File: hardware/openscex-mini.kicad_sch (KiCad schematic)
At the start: 11 parts, among them J1 ISP, U1 ATtiny85-20PU

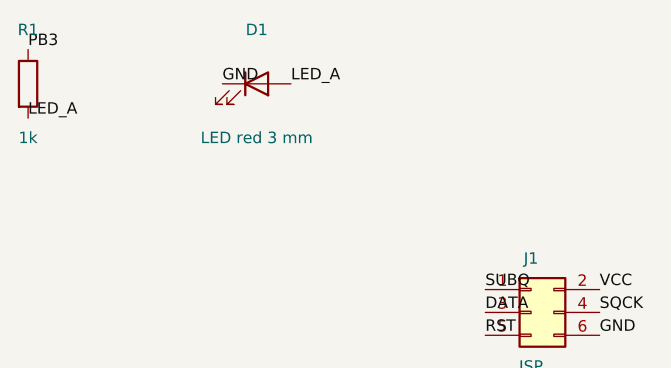
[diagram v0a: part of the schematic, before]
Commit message: feat(hardware): add a RESET pull-up to every board
The mini and bare boards now hold pin 1 high with a 10 kOhm pull-up,
as the carrier already did. The chip's own pull-up is 30 to 60 kOhm,
weak against noise coupled in from the console, and a spurious reset
costs the region check of the disc being read. Any ISP programmer
still overrides it.
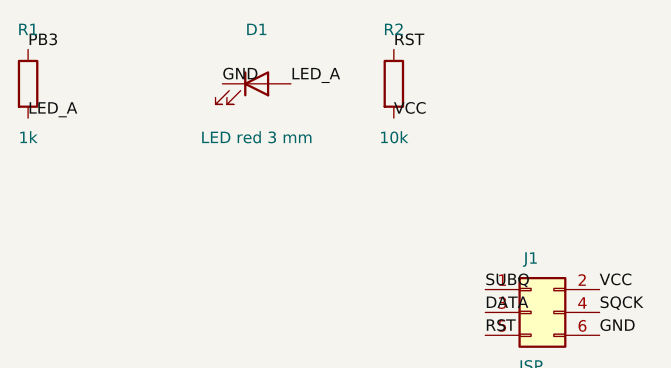
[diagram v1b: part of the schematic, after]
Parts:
- added R2: 10k, Resistor_THT:R_Axial_DIN0204_L3.6mm_D1.6mm_P5.08mm_Horizontal, symbol Device:R
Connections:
- net RST: now also R2.1
- net VCC: now also R2.2
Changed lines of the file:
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@@
 (kicad_sch (version 20231120) (generator "eeschema") (generator_version "8.0")
 	(paper "A3")
-	(title_block (title "openscex mini") (comment 1 "ATtiny85 PS1 modchip minimal carrier: socket, decoupling, LED, ISP"))
+	(title_block (title "openscex mini") (comment 1 "ATtiny85 PS1 modchip minimal carrier: socket, decoupling, RESET pull-up, LED, ISP"))
 (symbol (lib_id "MCU_Microchip_ATtiny:ATtiny85-20P") (at 76.2 76.2 0) (unit 1)
 	(in_bom yes) (on_board yes) (dnp no)
@@
 (label "VCC" (at 38.1 72.39 0) (effects (font (size 1.27 1.27)) (justify left bottom)))
 (label "GND" (at 38.1 80.01 0) (effects (font (size 1.27 1.27)) (justify left bottom)))
+(symbol (lib_id "Device:R") (at 167.64000000000001 50.8 0) (unit 1)
+	(in_bom yes) (on_board yes) (dnp no)
+	(property "Reference" "R2" (at 167.64000000000001 44.8 0) (effects (font (size 1.27 1.27))))
+	(property "Value" "10k" (at 167.64000000000001 56.8 0) (effects (font (size 1.27 1.27))))
+	(property "Footprint" "Resistor_THT:R_Axial_DIN0204_L3.6mm_D1.6mm_P5.08mm_Horizontal" (at 167.64000000000001 50.8 0) (effects (font (size 1.27 1.27)) (hide yes)))
+	(property "Datasheet" "" (at 167.64000000000001 50.8 0) (effects (font (size 1.27 1.27)) (hide yes)))
+	(property "Part" "10 kOhm axial resistor, DIN0204, 5.08 mm pitch" (at 167.64000000000001 50.8 0) (effects (font (size 1.27 1.27)) (hide yes)))
+	(pin "1")
+	(pin "2")
+	(instances (project "openscex-mini" (path "/7206801e-1c20-5311-8a84-3899543930cc" (reference "R2") (unit 1))))
+)
+(label "RST" (at 167.64 46.99 0) (effects (font (size 1.27 1.27)) (justify left bottom)))
+(label "VCC" (at 167.64 54.61 0) (effects (font (size 1.27 1.27)) (justify left bottom)))
 (symbol (lib_id "Device:R") (at 127.0 50.8 0) (unit 1)
 	(in_bom yes) (on_board yes) (dnp no)

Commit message: feat(hardware): name datasheet-checked parts
Every BOM line now names an exact manufacturer part, each checked
against its own datasheet: Microchip ATTINY85-20PU in a TE
1-2199298-2 socket, KEMET C315C104K5R5TA, Panasonic EEU-FC1A101S,
Vishay MBA0204 resistors, onsemi 2N3904RLRAG and 1N4148TR,
Kingbright WP710A10ID, CTS 206-2ST, Same Sky CMI-1295IC-0385T and
Wurth 61200621621.

C1 moves to a 4.0 x 2.5 mm footprint that fits the KEMET body. A
project footprint library, hardware/openscex.pretty, carries the hole
sizes the Wurth header and the buzzer datasheets recommend, 1.1 mm and
0.8 mm in 2 mm pads.
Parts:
- C1: footprint Capacitor_THT:C_Disc_D3.0mm_W1.6mm_P2.50mm -> Capacitor_THT:C_Rect_L4.0mm_W2.5mm_P2.50mm; Part 100 nF ceramic disc, 50 V, 2.5 mm pitch -> KEMET C315C104K5R5TA, 100 nF 50 V X7R, 2.54 mm
- D1: Part 3 mm red LED -> Kingbright WP710A10ID, 3 mm red LED
- J1: footprint Connector_IDC:IDC-Header_2x03_P2.54mm_Vertical -> openscex:IDC-Header_2x03_P2.54mm_Vertical_Wurth_61200621621; Part 2x3 shrouded box header, 2.54 mm, vertical -> Wurth 61200621621, 2x3 box header, 2.54 mm
- R1: Part 1 kOhm axial resistor, DIN0204, 5.08 mm pitch -> Vishay MBA02040C1001FC100, 1 kOhm 1 % 0.4 W, 0204
- R2: Part 10 kOhm axial resistor, DIN0204, 5.08 mm pitch -> Vishay MBA02040C1002FC100, 10 kOhm 1 % 0.4 W, 0204
- U1: Part ATtiny85-20PU in a DIP-8 7.62 mm socket -> Microchip ATTINY85-20PU in a TE 1-2199298-2 DIP-8 socket
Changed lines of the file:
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@@
 	(property "Footprint" "Package_DIP:DIP-8_W7.62mm_Socket" (at 76.2 76.2 0) (effects (font (size 1.27 1.27)) (hide yes)))
 	(property "Datasheet" "" (at 76.2 76.2 0) (effects (font (size 1.27 1.27)) (hide yes)))
-	(property "Part" "ATtiny85-20PU in a DIP-8 7.62 mm socket" (at 76.2 76.2 0) (effects (font (size 1.27 1.27)) (hide yes)))
+	(property "Part" "Microchip ATTINY85-20PU in a TE 1-2199298-2 DIP-8 socket" (at 76.2 76.2 0) (effects (font (size 1.27 1.27)) (hide yes)))
 	(pin "1")
 	(pin "2")
@@
 	(property "Reference" "C1" (at 38.1 70.2 0) (effects (font (size 1.27 1.27))))
 	(property "Value" "100nF" (at 38.1 82.2 0) (effects (font (size 1.27 1.27))))
-	(property "Footprint" "Capacitor_THT:C_Disc_D3.0mm_W1.6mm_P2.50mm" (at 38.1 76.2 0) (effects (font (size 1.27 1.27)) (hide yes)))
+	(property "Footprint" "Capacitor_THT:C_Rect_L4.0mm_W2.5mm_P2.50mm" (at 38.1 76.2 0) (effects (font (size 1.27 1.27)) (hide yes)))
 	(property "Datasheet" "" (at 38.1 76.2 0) (effects (font (size 1.27 1.27)) (hide yes)))
-	(property "Part" "100 nF ceramic disc, 50 V, 2.5 mm pitch" (at 38.1 76.2 0) (effects (font (size 1.27 1.27)) (hide yes)))
+	(property "Part" "KEMET C315C104K5R5TA, 100 nF 50 V X7R, 2.54 mm" (at 38.1 76.2 0) (effects (font (size 1.27 1.27)) (hide yes)))
 	(pin "1")
 	(pin "2")
@@
 	(property "Footprint" "Resistor_THT:R_Axial_DIN0204_L3.6mm_D1.6mm_P5.08mm_Horizontal" (at 167.64000000000001 50.8 0) (effects (font (size 1.27 1.27)) (hide yes)))
 	(property "Datasheet" "" (at 167.64000000000001 50.8 0) (effects (font (size 1.27 1.27)) (hide yes)))
-	(property "Part" "10 kOhm axial resistor, DIN0204, 5.08 mm pitch" (at 167.64000000000001 50.8 0) (effects (font (size 1.27 1.27)) (hide yes)))
+	(property "Part" "Vishay MBA02040C1002FC100, 10 kOhm 1 % 0.4 W, 0204" (at 167.64000000000001 50.8 0) (effects (font (size 1.27 1.27)) (hide yes)))
 	(pin "1")
 	(pin "2")
@@
 	(property "Footprint" "Resistor_THT:R_Axial_DIN0204_L3.6mm_D1.6mm_P5.08mm_Horizontal" (at 127.0 50.8 0) (effects (font (size 1.27 1.27)) (hide yes)))
 	(property "Datasheet" "" (at 127.0 50.8 0) (effects (font (size 1.27 1.27)) (hide yes)))
-	(property "Part" "1 kOhm axial resistor, DIN0204, 5.08 mm pitch" (at 127.0 50.8 0) (effects (font (size 1.27 1.27)) (hide yes)))
+	(property "Part" "Vishay MBA02040C1001FC100, 1 kOhm 1 % 0.4 W, 0204" (at 127.0 50.8 0) (effects (font (size 1.27 1.27)) (hide yes)))
 	(pin "1")
 	(pin "2")
@@
 	(property "Footprint" "LED_THT:LED_D3.0mm" (at 152.4 50.8 0) (effects (font (size 1.27 1.27)) (hide yes)))
 	(property "Datasheet" "" (at 152.4 50.8 0) (effects (font (size 1.27 1.27)) (hide yes)))
-	(property "Part" "3 mm red LED" (at 152.4 50.8 0) (effects (font (size 1.27 1.27)) (hide yes)))
+	(property "Part" "Kingbright WP710A10ID, 3 mm red LED" (at 152.4 50.8 0) (effects (font (size 1.27 1.27)) (hide yes)))
 	(pin "1")
 	(pin "2")
@@
 	(property "Reference" "J1" (at 182.88 70.2 0) (effects (font (size 1.27 1.27))))
 	(property "Value" "ISP" (at 182.88 82.2 0) (effects (font (size 1.27 1.27))))
-	(property "Footprint" "Connector_IDC:IDC-Header_2x03_P2.54mm_Vertical" (at 182.88 76.2 0) (effects (font (size 1.27 1.27)) (hide yes)))
+	(property "Footprint" "openscex:IDC-Header_2x03_P2.54mm_Vertical_Wurth_61200621621" (at 182.88 76.2 0) (effects (font (size 1.27 1.27)) (hide yes)))
 	(property "Datasheet" "" (at 182.88 76.2 0) (effects (font (size 1.27 1.27)) (hide yes)))
-	(property "Part" "2x3 shrouded box header, 2.54 mm, vertical" (at 182.88 76.2 0) (effects (font (size 1.27 1.27)) (hide yes)))
+	(property "Part" "Wurth 61200621621, 2x3 box header, 2.54 mm" (at 182.88 76.2 0) (effects (font (size 1.27 1.27)) (hide yes)))
 	(pin "1")
 	(pin "2")
